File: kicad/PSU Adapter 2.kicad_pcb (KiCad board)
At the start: 2 copper layers, 55 x 80 mm, 18 parts, among them J1 AC Connector, J2 Power to PSU, J3 Power to Logic Board, J4 Fan, J5 ATX From PSU, J6 Conn_01x05_Pin, K1 AC Passthrough Relay, U1 TLP521-1

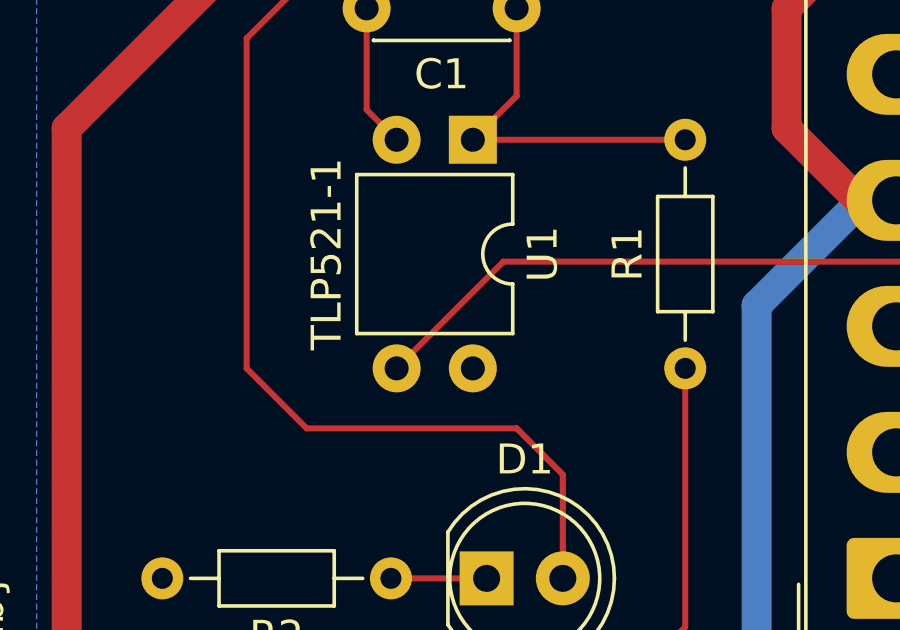
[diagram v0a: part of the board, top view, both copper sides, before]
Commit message: Add files via upload
Fix soft start
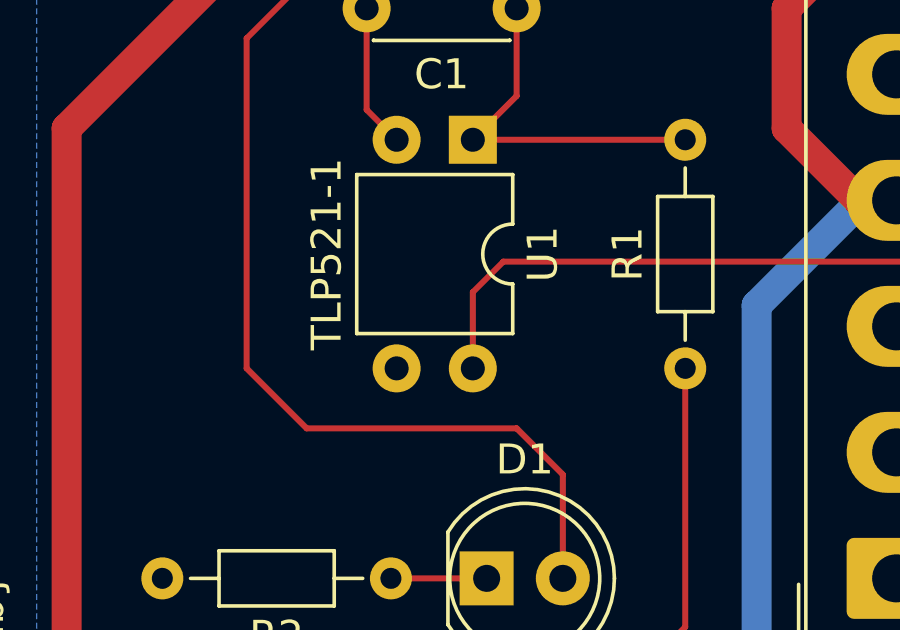
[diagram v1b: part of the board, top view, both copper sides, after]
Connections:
- U1 pad 3: /PS_ON -> /GND
- U1 pad 4: /GND -> /PS_ON
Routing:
- net /PS_ON: track 23.3 -> 22.3 mm
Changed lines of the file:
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@@
 	(property "Designer" "Rod Thomas")
 	(property "Github" "https://github.com/roddersuk/Apple-IIcx-PSU-ATX-Adapter")
-	(property "Revision" "0.3")
+	(property "Revision" "0.4")
 	(property "Title" "Apple Mac IIcx PSU ATX Adapter")
 	(net 0 "")
@@
 			(layers "*.Cu" "*.Mask")
 			(remove_unused_layers no)
-			(net 22 "/PS_ON")
+			(net 11 "/GND")
 			(pintype "passive")
 		)
@@
 			(layers "*.Cu" "*.Mask")
 			(remove_unused_layers no)
-			(net 11 "/GND")
+			(net 22 "/PS_ON")
 			(pintype "passive")
 		)
@@
 			(layers "*.Cu" "*.Mask")
 			(remove_unused_layers no)
-			(net 20 "unconnected-(J5-+3.3V-Pad1)_2")
+			(net 19 "unconnected-(J5-+3.3V-Pad1)_1")
 			(pinfunction "+3.3V")
 			(pintype "passive+no_connect")
@@
 			(layers "*.Cu" "*.Mask")
 			(remove_unused_layers no)
-			(net 23 "unconnected-(J5-+3.3V-Pad1)_3")
+			(net 20 "unconnected-(J5-+3.3V-Pad1)_2")
 			(pinfunction "+3.3V")
 			(pintype "passive+no_connect")
@@
 			(layers "*.Cu" "*.Mask")
 			(remove_unused_layers no)
-			(net 19 "unconnected-(J5-+3.3V-Pad1)_1")
+			(net 23 "unconnected-(J5-+3.3V-Pad1)_3")
 			(pinfunction "+3.3V")
 			(pintype "passive+no_connect")
@@
 	)
 	(segment
-		(start 140.975 129.975)
+		(start 144.532898 126.417102)
+		(end 159.932898 126.417102)
+		(width 0.2)
+		(layer "F.Cu")
+		(net 22)
+	)
+	(segment
+		(start 143.515 127.435)
 		(end 144.532898 126.417102)
 		(width 0.2)
@@
 	)
 	(segment
-		(start 144.532898 126.417102)
-		(end 159.932898 126.417102)
+		(start 143.515 129.975)
+		(end 143.515 127.435)
 		(width 0.2)
 		(layer "F.Cu")
